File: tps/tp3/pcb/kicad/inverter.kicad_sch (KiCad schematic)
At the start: 51 parts, among them J1 5Vext In, J2 Motor, J3 220Vac In, J4 15Vext In, Q1 IRF820, Q2 IRF820, Q3 IRF820, Q4 IRF820, Q5 IRF820, Q6 IRF820, U1 IR2110-A, U2 ESP32-DEVKIT-V1, U3 IR2110-B, U4 IR2110-C

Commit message: refactor inverter sch: replace VIC labels with  VDRV labels
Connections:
- net VIC is gone; now on net VDRV: C6.1, C9.1, D2.2 (A), D3.2 (A), U3.3 (VCC), U4.3 (VCC)
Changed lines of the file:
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@@
 	)
 	(symbol
-		(lib_id "power:VDC")
-		(at 60.96 168.91 270)
-		(unit 1)
-		(exclude_from_sim no)
-		(in_bom yes)
-		(on_board yes)
-		(dnp no)
-		(fields_autoplaced yes)
-		(property "Reference" "#PWR028"
-			(at 57.15 168.91 0)
-			(effects
-				(font
-					(size 1.27 1.27)
-				)
-				(hide yes)
-			)
-		)
-		(property "Value" "VIC"
-			(at 64.77 168.9099 90)
-			(effects
-				(font
-					(size 1.27 1.27)
-				)
-				(justify left)
-			)
-		)
-		(property "Footprint" ""
-			(at 60.96 168.91 0)
-			(effects
-				(font
-					(size 1.27 1.27)
-				)
-				(hide yes)
-			)
-		)
-		(property "Datasheet" ""
-			(at 60.96 168.91 0)
-			(effects
-				(font
-					(size 1.27 1.27)
-				)
-				(hide yes)
-			)
-		)
-		(property "Description" "Power symbol creates a global label with name \"VDC\""
-			(at 60.96 168.91 0)
-			(effects
-				(font
-					(size 1.27 1.27)
-				)
-				(hide yes)
-			)
-		)
-		(pin "1"
-		)
-		(instances
-			(project "inverter"
-				(path "/e9816699-297a-4648-9c1f-521bc7b67ea4"
-					(reference "#PWR028")
-					(unit 1)
-				)
-			)
-		)
-	)
-	(symbol
 		(lib_id "power:GND")
 		(at 229.87 116.84 0)
@@
 	)
 	(symbol
+		(lib_id "power:VDC")
+		(at 60.96 110.49 270)
+		(unit 1)
+		(exclude_from_sim no)
+		(in_bom yes)
+		(on_board yes)
+		(dnp no)
+		(fields_autoplaced yes)
+		(property "Reference" "#PWR018"
+			(at 57.15 110.49 0)
+			(effects
+				(font
+					(size 1.27 1.27)
+				)
+				(hide yes)
+			)
+		)
+		(property "Value" "VDRV"
+			(at 64.77 110.4899 90)
+			(effects
+				(font
+					(size 1.27 1.27)
+				)
+				(justify left)
+			)
+		)
+		(property "Footprint" ""
+			(at 60.96 110.49 0)
+			(effects
+				(font
+					(size 1.27 1.27)
+				)
+				(hide yes)
+			)
+		)
+		(property "Datasheet" ""
+			(at 60.96 110.49 0)
+			(effects
+				(font
+					(size 1.27 1.27)
+				)
+				(hide yes)
+			)
+		)
+		(property "Description" "Power symbol creates a global label with name \"VDC\""
+			(at 60.96 110.49 0)
+			(effects
+				(font
+					(size 1.27 1.27)
+				)
+				(hide yes)
+			)
+		)
+		(pin "1"
+		)
+		(instances
+			(project "inverter"
+				(path "/e9816699-297a-4648-9c1f-521bc7b67ea4"
+					(reference "#PWR018")
+					(unit 1)
+				)
+			)
+		)
+	)
+	(symbol
 		(lib_id "power:VD")
 		(at 224.79 21.59 0)
@@
 	)
 	(symbol
-		(lib_id "power:VDC")
-		(at 58.42 146.05 0)
-		(unit 1)
-		(exclude_from_sim no)
-		(in_bom yes)
-		(on_board yes)
-		(dnp no)
-		(fields_autoplaced yes)
-		(property "Reference" "#PWR026"
-			(at 58.42 149.86 0)
-			(effects
-				(font
-					(size 1.27 1.27)
-				)
-				(hide yes)
-			)
-		)
-		(property "Value" "VIC"
-			(at 58.42 140.97 0)
-			(effects
-				(font
-					(size 1.27 1.27)
-				)
-			)
-		)
-		(property "Footprint" ""
-			(at 58.42 146.05 0)
-			(effects
-				(font
-					(size 1.27 1.27)
-				)
-				(hide yes)
-			)
-		)
-		(property "Datasheet" ""
-			(at 58.42 146.05 0)
-			(effects
-				(font
-					(size 1.27 1.27)
-				)
-				(hide yes)
-			)
-		)
-		(property "Description" "Power symbol creates a global label with name \"VDC\""
-			(at 58.42 146.05 0)
-			(effects
-				(font
-					(size 1.27 1.27)
-				)
-				(hide yes)
-			)
-		)
-		(pin "1"
-		)
-		(instances
-			(project "inverter"
-				(path "/e9816699-297a-4648-9c1f-521bc7b67ea4"
-					(reference "#PWR026")
-					(unit 1)
-				)
-			)
-		)
-	)
-	(symbol
 		(lib_id "Device:C_Polarized")
 		(at 111.76 166.37 0)
@@
 	(symbol
 		(lib_id "power:VDC")
-		(at 60.96 110.49 270)
+		(at 60.96 168.91 270)
 		(unit 1)
 		(exclude_from_sim no)
@@
 		(dnp no)
 		(fields_autoplaced yes)
-		(property "Reference" "#PWR018"
-			(at 57.15 110.49 0)
+		(property "Reference" "#PWR028"
+			(at 57.15 168.91 0)
 			(effects
 				(font
@@
 			)
 		)
-		(property "Value" "VIC"
-			(at 64.77 110.4899 90)
+		(property "Value" "VDRV"
+			(at 64.77 168.9099 90)
 			(effects
 				(font
@@
 		)
 		(property "Footprint" ""
-			(at 60.96 110.49 0)
+			(at 60.96 168.91 0)
 			(effects
 				(font
@@
 		)
 		(property "Datasheet" ""
-			(at 60.96 110.49 0)
+			(at 60.96 168.91 0)
 			(effects
 				(font
@@
 		)
 		(property "Description" "Power symbol creates a global label with name \"VDC\""
-			(at 60.96 110.49 0)
+			(at 60.96 168.91 0)
 			(effects
 				(font
@@
 			(project "inverter"
 				(path "/e9816699-297a-4648-9c1f-521bc7b67ea4"
-					(reference "#PWR018")
+					(reference "#PWR028")
 					(unit 1)
 				)
@@
 	)
 	(symbol
+		(lib_id "power:VDC")
+		(at 58.42 146.05 0)
+		(unit 1)
+		(exclude_from_sim no)
+		(in_bom yes)
+		(on_board yes)
+		(dnp no)
+		(fields_autoplaced yes)
+		(property "Reference" "#PWR026"
+			(at 58.42 149.86 0)
+			(effects
+				(font
+					(size 1.27 1.27)
+				)
+				(hide yes)
+			)
+		)
+		(property "Value" "VDRV"
+			(at 58.42 140.97 0)
+			(effects
+				(font
+					(size 1.27 1.27)
+				)
+			)
+		)
+		(property "Footprint" ""
+			(at 58.42 146.05 0)
+			(effects
+				(font
+					(size 1.27 1.27)
+				)
+				(hide yes)
+			)
+		)
+		(property "Datasheet" ""
+			(at 58.42 146.05 0)
+			(effects
+				(font
+					(size 1.27 1.27)
+				)
+				(hide yes)
+			)
+		)
+		(property "Description" "Power symbol creates a global label with name \"VDC\""
+			(at 58.42 146.05 0)
+			(effects
+				(font
+					(size 1.27 1.27)
+				)
+				(hide yes)
+			)
+		)
+		(pin "1"
+		)
+		(instances
+			(project "inverter"
+				(path "/e9816699-297a-4648-9c1f-521bc7b67ea4"
+					(reference "#PWR026")
+					(unit 1)
+				)
+			)
+		)
+	)
+	(symbol
 		(lib_id "power:Earth")
 		(at 35.56 124.46 0)
@@
 	)
 	(symbol
-		(lib_id "power:VDC")
-		(at 58.42 87.63 0)
-		(unit 1)
-		(exclude_from_sim no)
-		(in_bom yes)
-		(on_board yes)
-		(dnp no)
-		(fields_autoplaced yes)
-		(property "Reference" "#PWR016"
-			(at 58.42 91.44 0)
-			(effects
-				(font
-					(size 1.27 1.27)
-				)
-				(hide yes)
-			)
-		)
-		(property "Value" "VIC"
-			(at 58.42 82.55 0)
-			(effects
-				(font
-					(size 1.27 1.27)
-				)
-			)
-		)
-		(property "Footprint" ""
-			(at 58.42 87.63 0)
-			(effects
-				(font
-					(size 1.27 1.27)
-				)
-				(hide yes)
-			)
-		)
-		(property "Datasheet" ""
-			(at 58.42 87.63 0)
-			(effects
-				(font
-					(size 1.27 1.27)
-				)
-				(hide yes)
-			)
-		)
-		(property "Description" "Power symbol creates a global label with name \"VDC\""
-			(at 58.42 87.63 0)
-			(effects
-				(font
-					(size 1.27 1.27)
-				)
-				(hide yes)
-			)
-		)
-		(pin "1"
-		)
-		(instances
-			(project "inverter"
-				(path "/e9816699-297a-4648-9c1f-521bc7b67ea4"
-					(reference "#PWR016")
-					(unit 1)
-				)
-			)
-		)
-	)
-	(symbol
 		(lib_id "Device:R")
 		(at 74.93 41.91 90)
@@
 					(unit 1)
 				)
+			)
+		)
+	)
+	(symbol
+		(lib_id "power:VDC")
+		(at 58.42 87.63 0)
+		(unit 1)
+		(exclude_from_sim no)
+		(in_bom yes)
+		(on_board yes)
+		(dnp no)
+		(fields_autoplaced yes)
+		(property "Reference" "#PWR016"
+			(at 58.42 91.44 0)
+			(effects
+				(font
+					(size 1.27 1.27)
+				)
+				(hide yes)
+			)
+		)
+		(property "Value" "VDRV"
+			(at 58.42 82.55 0)
+			(effects
+				(font
+					(size 1.27 1.27)
+				)
+			)
+		)
+		(property "Footprint" ""
+			(at 58.42 87.63 0)
+			(effects
+				(font
+					(size 1.27 1.27)
+				)
+				(hide yes)
+			)
+		)
+		(property "Datasheet" ""
+			(at 58.42 87.63 0)
+			(effects
+				(font
+					(size 1.27 1.27)
+				)
+				(hide yes)
+			)
+		)
+		(property "Description" "Power symbol creates a global label with name \"VDC\""
+			(at 58.42 87.63 0)
+			(effects
+				(font
+					(size 1.27 1.27)
+				)
+				(hide yes)
+			)
+		)
+		(pin "1"
+		)
+		(instances
+			(project "inverter"
+				(path "/e9816699-297a-4648-9c1f-521bc7b67ea4"
+					(reference "#PWR016")
+					(unit 1)
+				)

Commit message: inverter sch visual improvements
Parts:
- removed D8: Red, LED_THT:LED_D3.0mm, symbol Device:LED
- added C18: 1u-35V, Capacitor_THT:C_Disc_D4.3mm_W1.9mm_P5.00mm, symbol Device:C
- added C19: 10u, Capacitor_THT:CP_Radial_D5.0mm_P2.00mm, symbol Device:C_Polarized
- added D9: Red, LED_THT:LED_D3.0mm, symbol Device:LED
- added RV1: 10k, Potentiometer_THT:Potentiometer_Alps_RK163_Single_Horizontal, symbol Device:R_Potentiometer
- C13: value 10n-650V -> 10n-450V
- C14, C15, C16: value C_Polarized -> 33u-450V
- C17: value 22u -> 22u-35V
- C2, C6, C9: value 10u -> 1u
- R10, R11, R12: value 100k -> 150k
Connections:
- net COM: now also C18.2
- net VD: now also D9.2 (A)
- net VDD: now also C19.1, RV1.3
- net VDRV: now also C18.1
- net VSS: now also C19.2, RV1.1
- net at R10.2, R11.2, R12.2: now also D9.1 (K)
- net at U2.25 (D27): now also RV1.2
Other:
- note added: "220Vac"
- note added: "ADC2_7"
- note added: "Control Velocidad"
- moved on the sheet: C10, C11, C12, C13, C17, D4, D5, D6, D7, J1, J3, J4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

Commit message: Add Vd out
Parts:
- added C4: 47u-450V, Capacitor_THT:CP_Radial_D17.0mm_P7.50mm, symbol Device:C_Polarized
- added J2: Vd out, symbol Connector:Screw_Terminal_01x02
- renumbered C3 to C1, C4 to C10, C10 to C11, C19 to C12, C11 to C13, C5 to C14, C6 to C16, C7 to C17, C8 to C18, C16 to C19, C12 to C2, C9 to C20, C13 to C3, C1 to C5, C14 to C6, C2 to C7, C17 to C8, C18 to C9, D4 to D2, D9 to D3, D7 to D4, D2 to D5, D5 to D7, D3 to D8, J3 to J1, J4 to J3, J1 to J4, J2 to J5, R10 to R1, R7 to R10, R5 to R11, R6 to R12, R11 to R2, R12 to R3, R1 to R4, R2 to R5, R9 to R6, R3 to R7, R4 to R8, R8 to R9, U3 to U2, U2 to U3
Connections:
- net VSS is gone; now on net COM: C1.2, C10.2, C11.2, C12.2, C13.2, C17.2, J4.2 (Pin_2), R10.2, R9.2, RV1.1, U1.13 (VSS), U2.13 (VSS), U3.2 (GND), U3.29 (GND), U4.13 (VSS)
- net COM: now also C4.2, J2.2 (Pin_2)
- net VD: now also C4.1, J2.1 (Pin_1)
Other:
- moved on the sheet: C2, C3, D2, D3, J1, R1, R2, R3

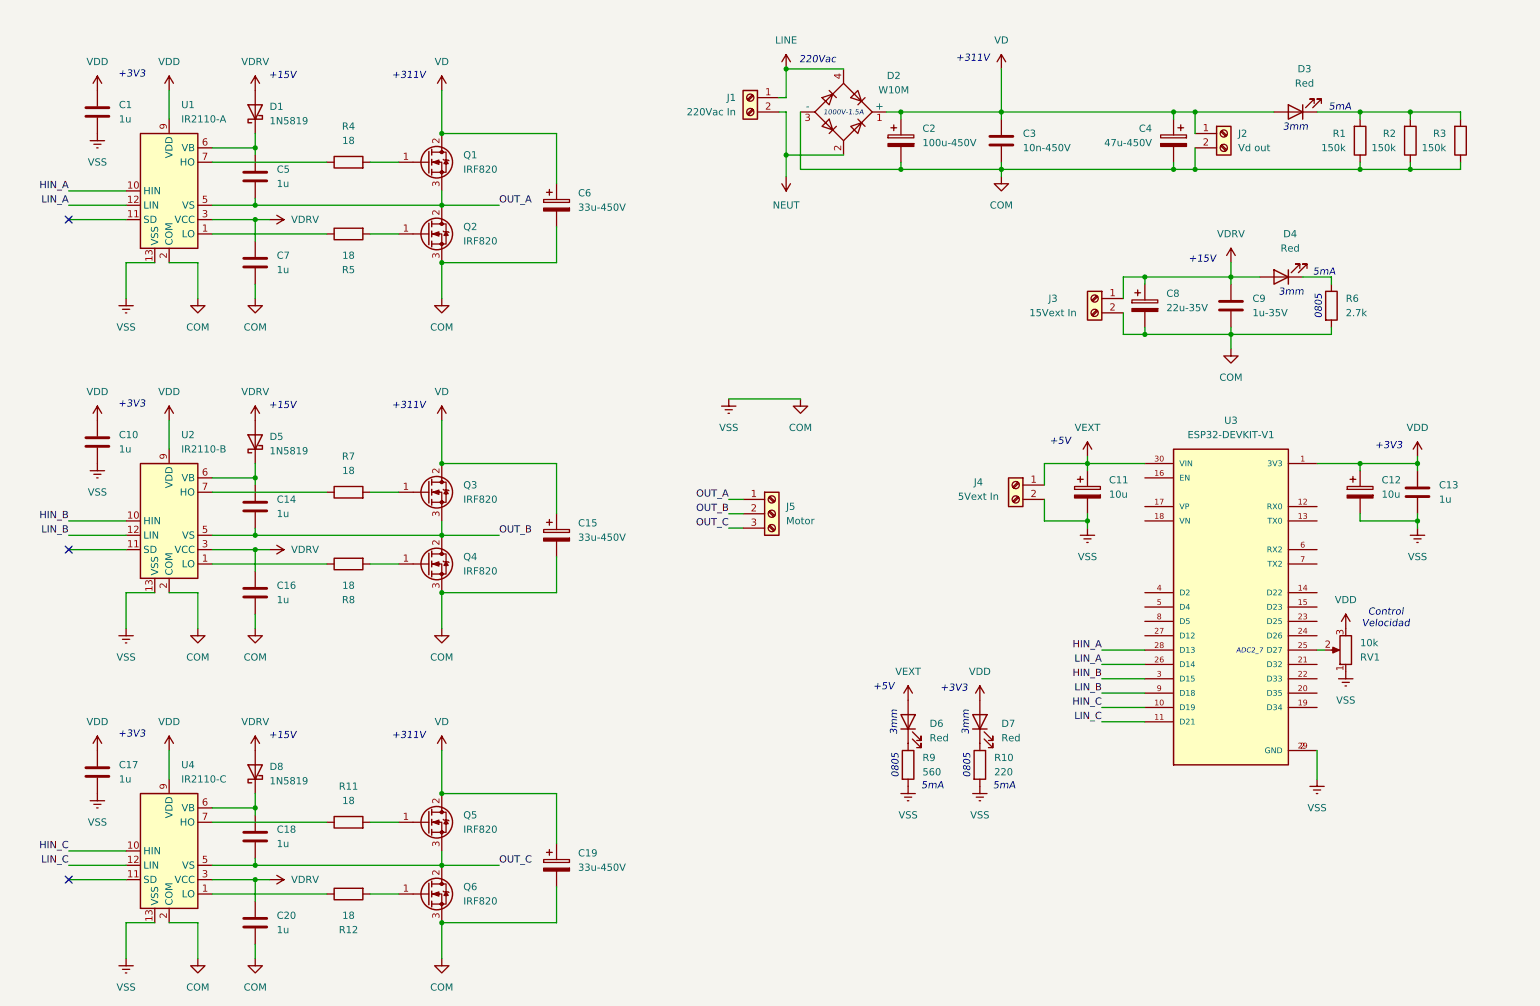
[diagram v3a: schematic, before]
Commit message: fix inverter sch after feedback and real component sizes, start PCB routing
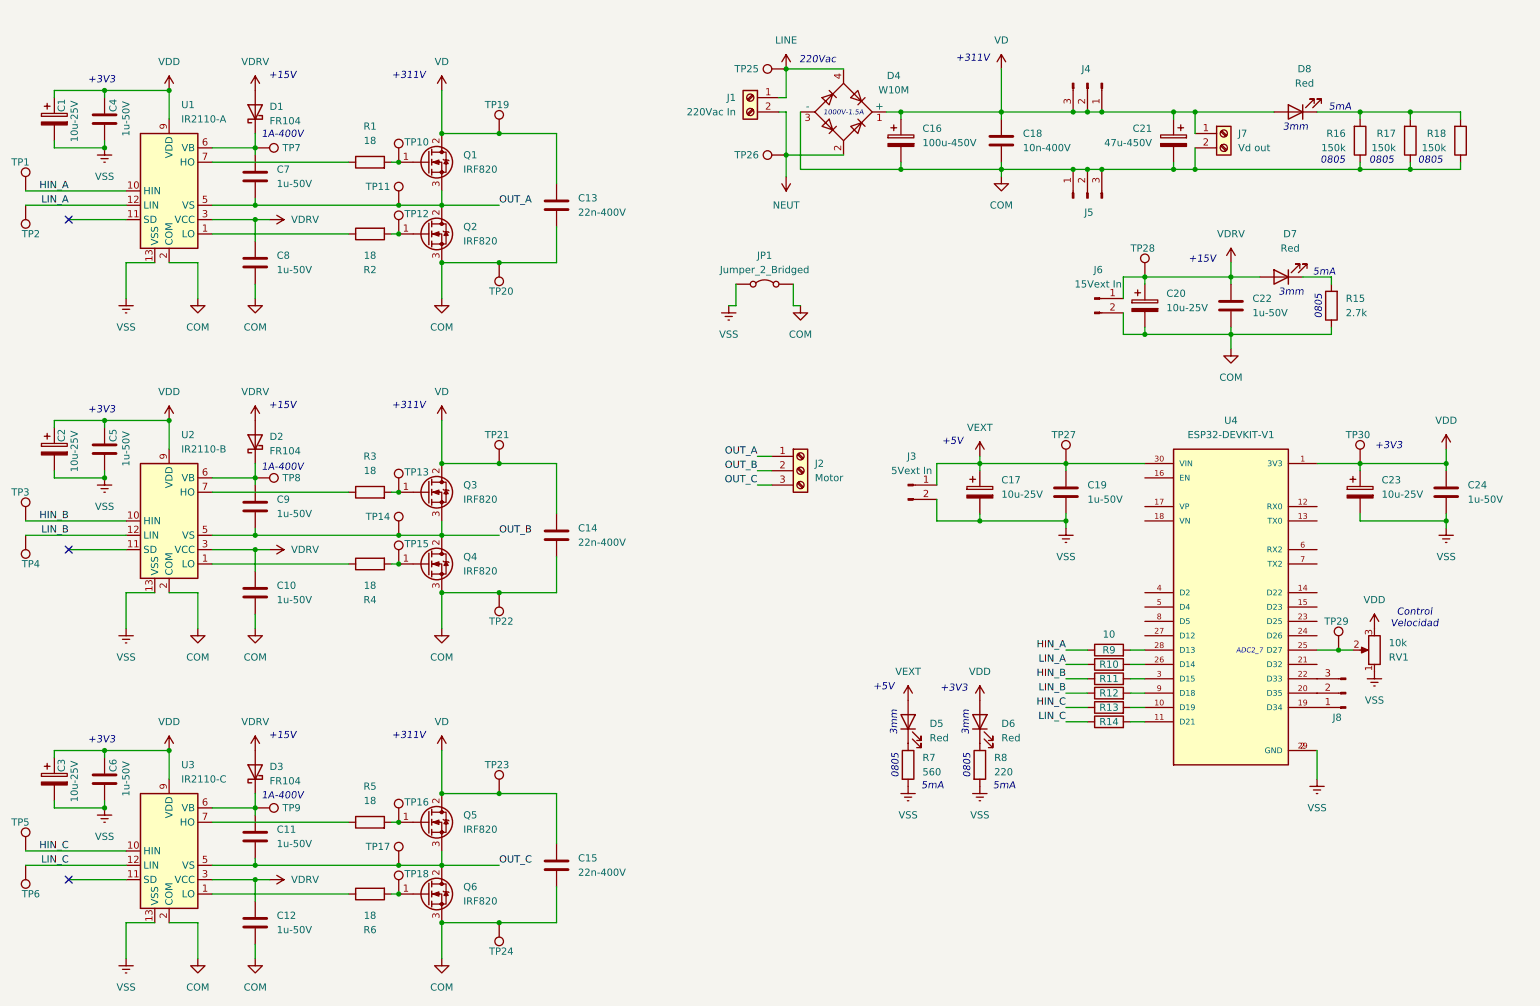
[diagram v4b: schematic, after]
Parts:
- removed C1, C10, C17: 1u, Capacitor_THT:C_Disc_D4.3mm_W1.9mm_P5.00mm, symbol Device:C
- removed C11, C12: 10u, Capacitor_THT:CP_Radial_D5.0mm_P2.00mm, symbol Device:C_Polarized
- removed C15, C19, C6: 33u-450V, symbol Device:C_Polarized
- removed C9: 1u-35V, Capacitor_THT:C_Disc_D4.3mm_W1.9mm_P5.00mm, symbol Device:C
- removed J3: 15Vext In, TerminalBlock:TerminalBlock_bornier-2_P5.08mm, symbol Connector:Screw_Terminal_01x02
- removed J4: 5Vext In, TerminalBlock:TerminalBlock_bornier-2_P5.08mm, symbol Connector:Screw_Terminal_01x02
- added C1, C17, C2, C23, C3: 10u-25V, Capacitor_THT:CP_Radial_D4.0mm_P1.50mm, symbol Device:C_Polarized
- added C13, C14, C15: 22n-400V, Capacitor_THT:C_Rect_L11.5mm_W4.0mm_P10.00mm_MKT, symbol Device:C
- added C19, C22, C4, C5, C6: 1u-50V, Capacitor_THT:C_Disc_D4.7mm_W2.5mm_P5.00mm, symbol Device:C
- added J3: 5Vext In, Connector_Molex:Molex_KK-254_AE-6410-02A_1x02_P2.54mm_Vertical, symbol Connector:Conn_01x02_Pin
- added J4, J5, J8: Conn_01x03_Pin, Connector_PinHeader_2.54mm:PinHeader_1x03_P2.54mm_Vertical, symbol Connector:Conn_01x03_Pin
- added J6: 15Vext In, Connector_Molex:Molex_KK-254_AE-6410-02A_1x02_P2.54mm_Vertical, symbol Connector:Conn_01x02_Pin
- added JP1: Jumper_2_Bridged, Jumper:SolderJumper-2_P1.3mm_Open_RoundedPad1.0x1.5mm, symbol Jumper:Jumper_2_Bridged
- added R10, R11, R12, R13, R14, R9: 10, Resistor_THT:R_Axial_DIN0207_L6.3mm_D2.5mm_P10.16mm_Horizontal, symbol Device:R
- added TP1, TP10, TP11, TP12, TP13, TP14, TP15, TP16, TP17, TP18, TP19, TP2, TP20, TP21, TP22, TP23, TP24, TP25, TP26, TP27, TP28, TP29, TP3, TP30, TP4, TP5, TP6, TP7, TP8, TP9: TestPoint, Connector_PinHeader_2.54mm:PinHeader_1x01_P2.54mm_Vertical, symbol Connector:TestPoint
- C10: renamed from C16; value 1u -> 1u-50V; footprint Capacitor_THT:C_Disc_D4.3mm_W1.9mm_P5.00mm -> Capacitor_THT:C_Disc_D4.7mm_W2.5mm_P5.00mm
- C11: renamed from C18; value 1u -> 1u-50V; footprint Capacitor_THT:C_Disc_D4.3mm_W1.9mm_P5.00mm -> Capacitor_THT:C_Disc_D4.7mm_W2.5mm_P5.00mm
- C12: renamed from C20; value 1u -> 1u-50V; footprint Capacitor_THT:C_Disc_D4.3mm_W1.9mm_P5.00mm -> Capacitor_THT:C_Disc_D4.7mm_W2.5mm_P5.00mm
- C18: renamed from C3; value 10n-450V -> 10n-400V; footprint Capacitor_THT:C_Rect_L27.0mm_W9.0mm_P22.00mm -> Capacitor_THT:C_Rect_L11.5mm_W4.5mm_P10.00mm_MKT
- C20: renamed from C8; value 22u-35V -> 10u-25V; footprint Capacitor_THT:CP_Radial_D5.0mm_P2.00mm -> Capacitor_THT:CP_Radial_D4.0mm_P1.50mm
- C21: renamed from C4; footprint Capacitor_THT:CP_Radial_D17.0mm_P7.50mm -> Capacitor_THT:CP_Radial_D16.0mm_P7.50mm
- C24: renamed from C13; value 1u -> 1u-50V; footprint Capacitor_THT:C_Disc_D4.3mm_W1.9mm_P5.00mm -> Capacitor_THT:C_Disc_D4.7mm_W2.5mm_P5.00mm
- C7: renamed from C5; value 1u -> 1u-50V; footprint Capacitor_THT:C_Disc_D4.3mm_W1.9mm_P5.00mm -> Capacitor_THT:C_Disc_D4.7mm_W2.5mm_P5.00mm
- C8: renamed from C7; value 1u -> 1u-50V; footprint Capacitor_THT:C_Disc_D4.3mm_W1.9mm_P5.00mm -> Capacitor_THT:C_Disc_D4.7mm_W2.5mm_P5.00mm
- C9: renamed from C14; value 1u -> 1u-50V; footprint Capacitor_THT:C_Disc_D4.3mm_W1.9mm_P5.00mm -> Capacitor_THT:C_Disc_D4.7mm_W2.5mm_P5.00mm
- D1: value 1N5819 -> FR104
- D2: renamed from D5; value 1N5819 -> FR104
- D3: renamed from D8; value 1N5819 -> FR104
- J7: renamed from J2; footprint (none) -> TerminalBlock:TerminalBlock_bornier-2_P5.08mm
- R1: renamed from R4; footprint Resistor_THT:R_Axial_DIN0207_L6.3mm_D2.5mm_P15.24mm_Horizontal -> Resistor_THT:R_Axial_DIN0204_L3.6mm_D1.6mm_P7.62mm_Horizontal
- R16: renamed from R1; footprint Resistor_THT:R_Axial_DIN0207_L6.3mm_D2.5mm_P15.24mm_Horizontal -> Resistor_SMD:R_0805_2012Metric_Pad1.20x1.40mm_HandSolder
- R17: renamed from R2; footprint Resistor_THT:R_Axial_DIN0207_L6.3mm_D2.5mm_P15.24mm_Horizontal -> Resistor_SMD:R_0805_2012Metric_Pad1.20x1.40mm_HandSolder
- R18: renamed from R3; footprint Resistor_THT:R_Axial_DIN0207_L6.3mm_D2.5mm_P15.24mm_Horizontal -> Resistor_SMD:R_0805_2012Metric_Pad1.20x1.40mm_HandSolder
- R2: renamed from R5; footprint Resistor_THT:R_Axial_DIN0207_L6.3mm_D2.5mm_P15.24mm_Horizontal -> Resistor_THT:R_Axial_DIN0204_L3.6mm_D1.6mm_P7.62mm_Horizontal
- R3: renamed from R7; footprint Resistor_THT:R_Axial_DIN0207_L6.3mm_D2.5mm_P15.24mm_Horizontal -> Resistor_THT:R_Axial_DIN0204_L3.6mm_D1.6mm_P7.62mm_Horizontal
- R4: renamed from R8; footprint Resistor_THT:R_Axial_DIN0207_L6.3mm_D2.5mm_P15.24mm_Horizontal -> Resistor_THT:R_Axial_DIN0204_L3.6mm_D1.6mm_P7.62mm_Horizontal
- R5: renamed from R11; footprint Resistor_THT:R_Axial_DIN0207_L6.3mm_D2.5mm_P15.24mm_Horizontal -> Resistor_THT:R_Axial_DIN0204_L3.6mm_D1.6mm_P7.62mm_Horizontal
- R6: renamed from R12; footprint Resistor_THT:R_Axial_DIN0207_L6.3mm_D2.5mm_P15.24mm_Horizontal -> Resistor_THT:R_Axial_DIN0204_L3.6mm_D1.6mm_P7.62mm_Horizontal
- renumbered C2 to C16, D2 to D4, D6 to D5, D7 to D6, D4 to D7, D3 to D8, J5 to J2, R6 to R15, R9 to R7, R10 to R8, U4 to U3, U3 to U4
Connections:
- net COM: now also R15.1, C13.2, C14.2, C15.2, C22.2, J5.1 (Pin_1), J5.2 (Pin_2), J5.3 (Pin_3), J6.2 (Pin_2), JP1.2 (B), TP20.1, TP22.1, TP24.1; no longer C24.2, R15.2, R7.2, R8.2, RV1.1, U1.13 (VSS), U2.13 (VSS), U3.13 (VSS), U4.2 (GND), U4.29 (GND)
- net HIN_A: now also R9.1, TP1.1; no longer U4.28 (D13)
- net HIN_B: now also R11.1, TP3.1; no longer U4.3 (D15)
- net HIN_C: now also R13.1, TP5.1; no longer U4.10 (D19)
- net LINE: now also TP25.1
- net LIN_A: now also R10.1, TP2.1; no longer U4.26 (D14)
- net LIN_B: now also R12.1, TP4.1; no longer U4.9 (D18)
- net LIN_C: now also R14.1, TP6.1; no longer U4.11 (D21)
- net NEUT: now also TP26.1
- net OUT_A: now also TP11.1
- net OUT_B: now also TP14.1
- net OUT_C: now also TP17.1
- net VD: now also C13.1, C14.1, C15.1, J4.1 (Pin_1), J4.2 (Pin_2), J4.3 (Pin_3), TP19.1, TP21.1, TP23.1
- net VDD: now also C1.1, C2.1, C23.1, C3.1, C4.1, C5.1, C6.1, TP30.1
- net VDRV: now also C22.1, J6.1 (Pin_1), TP28.1
- net VEXT: now also C17.1, C19.1, J3.1 (Pin_1), TP27.1
- net at C7.1, D1.1 (K), U1.6 (VB): now also TP7.1
- net at Q5.1 (G), R5.2: now also TP16.1
- net at D7.1 (K): now also R15.2; no longer R15.1
- net at Q3.1 (G), R3.2: now also TP13.1
- net at C11.1, D3.1 (K), U3.6 (VB): now also TP9.1
- net at C9.1, D2.1 (K), U2.6 (VB): now also TP8.1
- net at Q1.1 (G), R1.2: now also TP10.1
- net at Q2.1 (G), R2.2: now also TP12.1
- net at Q6.1 (G), R6.2: now also TP18.1
- net at Q4.1 (G), R4.2: now also TP15.1
- net at RV1.2, U4.25 (D27): now also TP29.1
- net at U4.19 (D34): now also J8.1 (Pin_1)
- net at U4.20 (D35): now also J8.2 (Pin_2)
- net at U4.22 (D33): now also J8.3 (Pin_3)
- new net: R13.2, U4.10 (D19)
- new net: R10.2, U4.26 (D14)
- new net: R11.2, U4.3 (D15)
- new net: R9.2, U4.28 (D13)
- new net: R14.2, U4.11 (D21)
- new net: R12.2, U4.9 (D18)
- new net VSS: C1.2, C17.2, C19.2, C2.2, C23.2, C24.2, C3.2, C4.2, C5.2, C6.2, J3.2 (Pin_2), JP1.1 (A), R7.2, R8.2, RV1.1, U1.13 (VSS), U2.13 (VSS), U3.13 (VSS), U4.2 (GND), U4.29 (GND)
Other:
- note added: "1A-400V"
- moved on the sheet: C24, J2, R1, R15, R2, R3, R4, R5, R6, RV1
